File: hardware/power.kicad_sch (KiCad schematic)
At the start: 36 parts, among them Q1 DMN1150UFB-7B, U13 TPS746-3.3DRV, U21 NCV8187AMT180TAG, U33 TPS2116DRLR, U6 LMR51420YDDCR, U7 LMR51420YDDCR

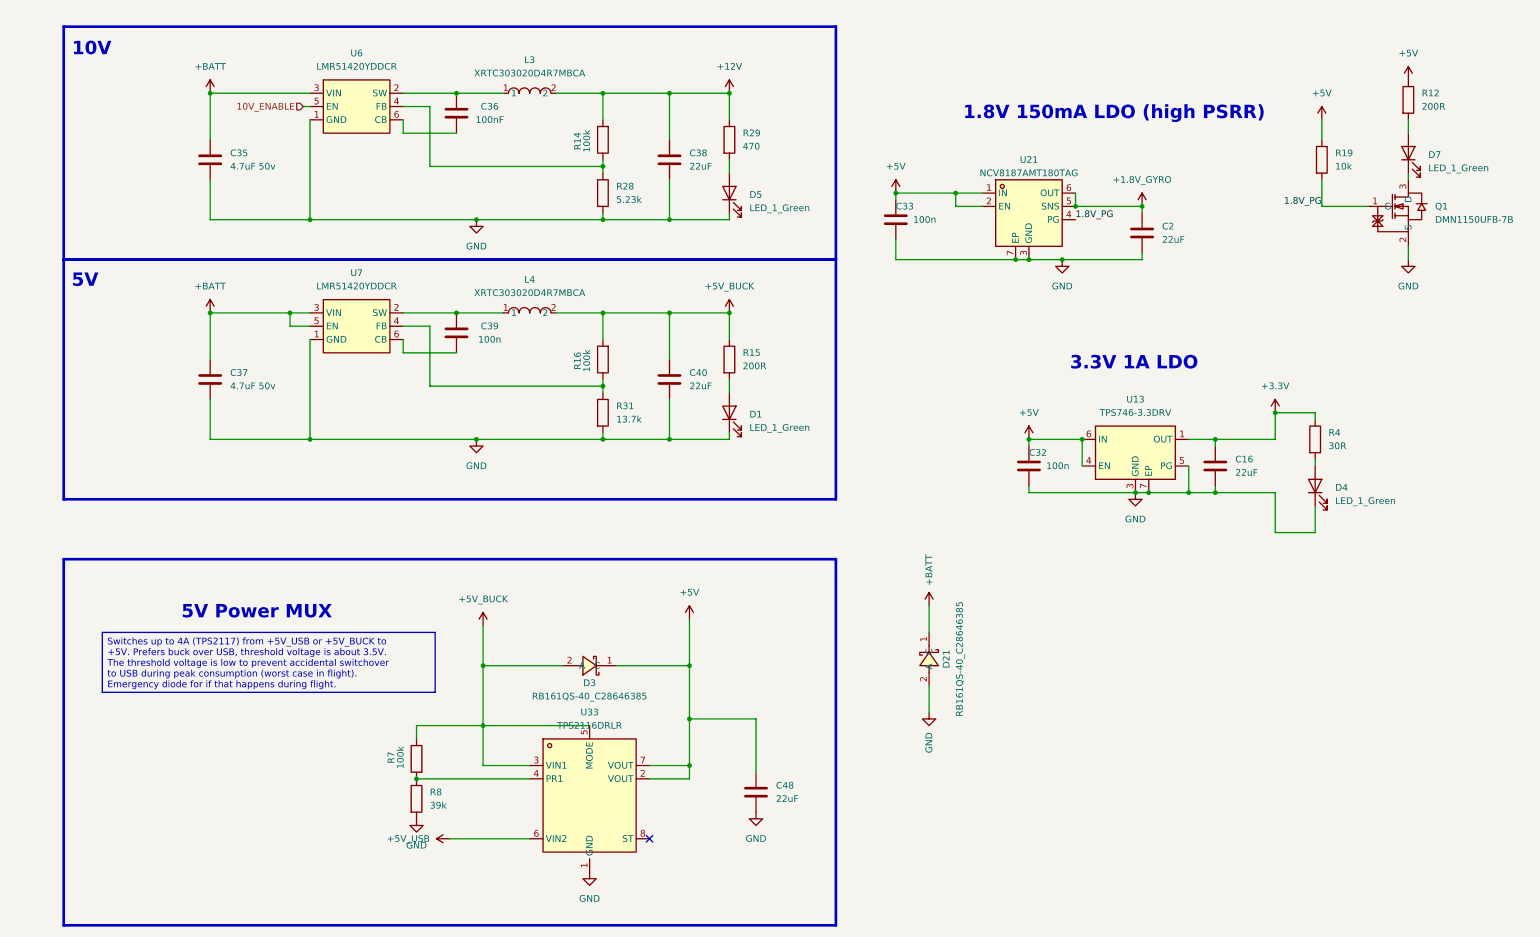
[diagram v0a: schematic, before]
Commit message: switched to 0201
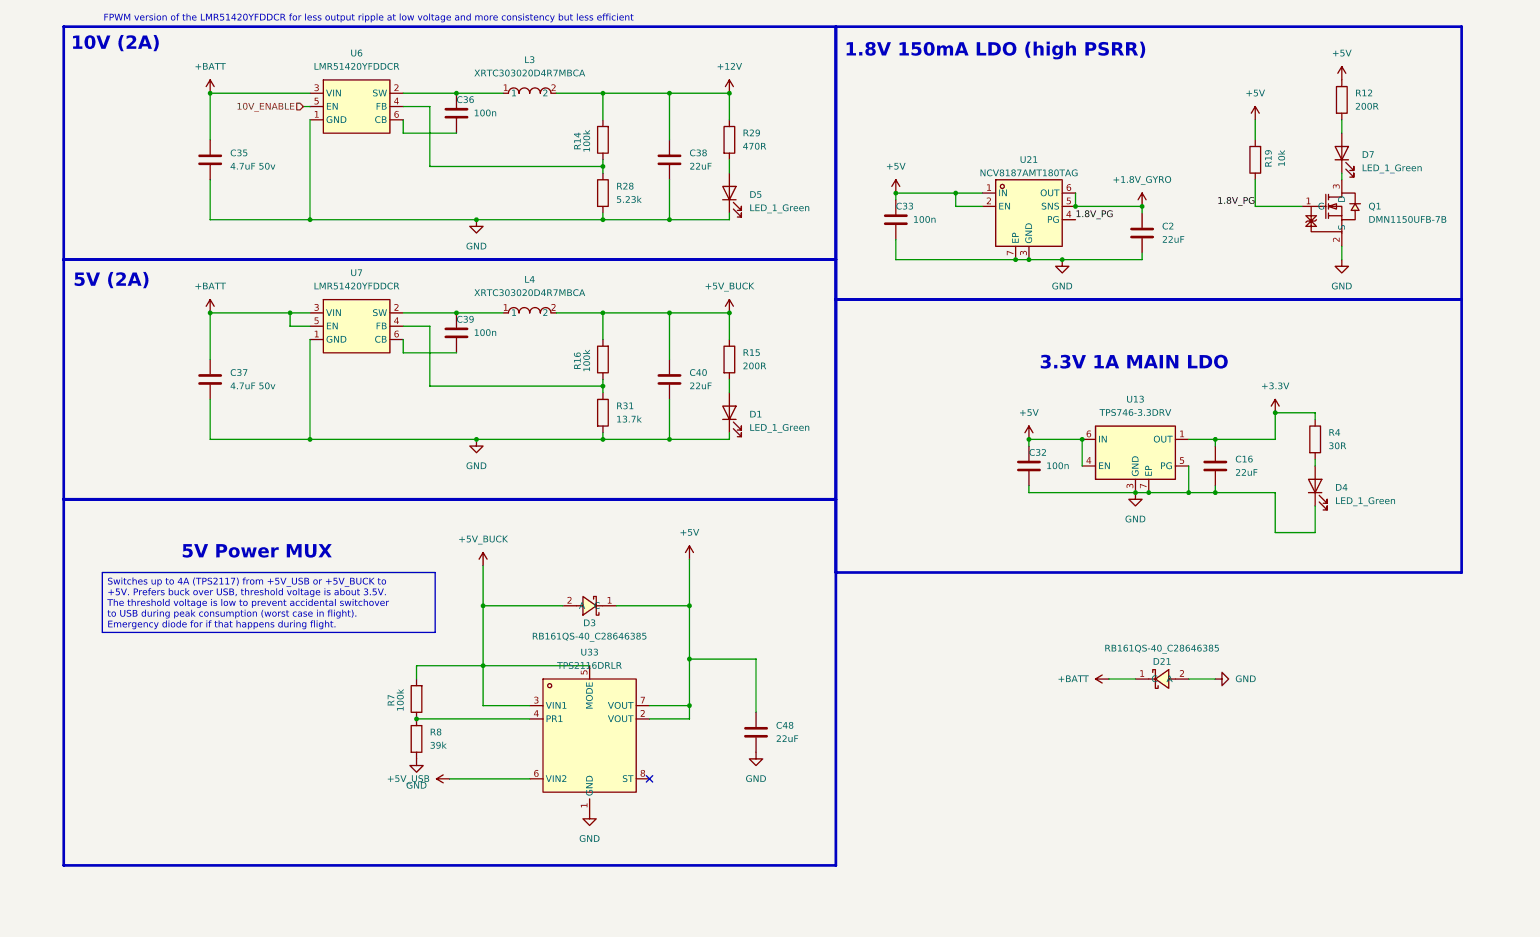
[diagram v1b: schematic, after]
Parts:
- C32, C33, C39: footprint Capacitor_SMD:C_0402_1005Metric -> Capacitor_SMD:C_0201_0603Metric; LCSC C1525 -> C76939
- C36: value 100nF -> 100n; footprint Capacitor_SMD:C_0402_1005Metric -> Capacitor_SMD:C_0201_0603Metric; LCSC C1525 -> C76939
- R12, R15: footprint Resistor_SMD:R_0402_1005Metric -> Capacitor_SMD:C_0201_0603Metric; LCSC C25087 -> C270359
- R14, R16, R7: footprint Resistor_SMD:R_0402_1005Metric -> Capacitor_SMD:C_0201_0603Metric; LCSC C60491 -> C270364
- R19: footprint Resistor_SMD:R_0402_1005Metric -> Capacitor_SMD:C_0201_0603Metric; LCSC C25087 -> C473048
- R28: footprint Resistor_SMD:R_0402_1005Metric -> Capacitor_SMD:C_0201_0603Metric; LCSC C2684530 -> C851767
- R29: value 470 -> 470R; footprint Resistor_SMD:R_0402_1005Metric -> Capacitor_SMD:C_0201_0603Metric; LCSC C114877 -> C473464
- R31: footprint Resistor_SMD:R_0402_1005Metric -> Capacitor_SMD:C_0201_0603Metric; LCSC C2933072 -> C138175
- R4: footprint Resistor_SMD:R_0402_1005Metric -> Capacitor_SMD:C_0201_0603Metric; LCSC C138007 -> C778391
- R8: footprint Resistor_SMD:R_0402_1005Metric -> Capacitor_SMD:C_0201_0603Metric; LCSC C137995 -> C473053
- U6, U7: value LMR51420YDDCR -> LMR51420YFDDCR; LCSC Part C5383002 -> C7296200
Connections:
- net +5V: now also R19.2; no longer R19.1
- net +5V_BUCK: now also R7.2; no longer R7.1
- net 1.8V_PG: now also R19.1; no longer R19.2
- net at R8.1, U33.4 (PR1): now also R7.1; no longer R7.2
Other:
- note added: "10V (2A)"
- note added: "3.3V 1A MAIN LDO"
- note added: "5V (2A)"
- note added: "FPWM version of the LMR51420YFDDCR for less output ripple at low voltage and more consistency but less efficient"
- note removed: "10V"
- note removed: "3.3V 1A LDO"
- note removed: "5V"
- moved on the sheet: C48, D21, D3, D7, Q1, R8, U33
